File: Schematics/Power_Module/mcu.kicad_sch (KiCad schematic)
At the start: 39 parts, among them J1 USB_C_Female_USB2_Small, J4 SWD_B, J5 Stack Male Edge Connector, SW1 SW_STM_BOOT_MODE, SW3 SW_STM_RESET, U11 W25Q128JVS, U12 CP2102N-Axx-xQFN20, U13 ISO1044BDR, U9 STM32F103CBT6, Y1 X322516MMB4SI

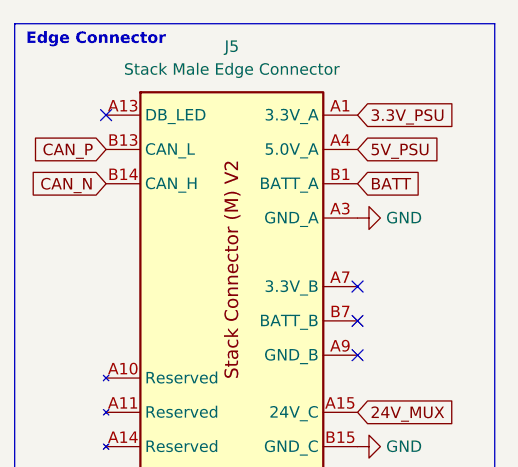
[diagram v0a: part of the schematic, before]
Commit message: adding power ORing circuit
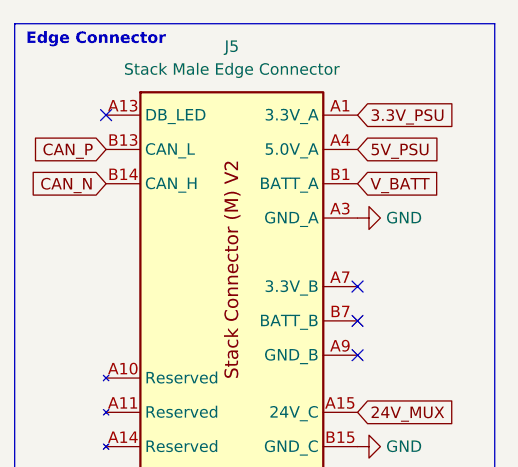
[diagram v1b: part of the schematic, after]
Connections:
- net BATT renamed V_BATT
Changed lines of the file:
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@@
 		)
 	)
-	(global_label "BATT"
+	(global_label "V_BATT"
 		(shape input)
 		(at 269.24 30.48 0)
@@
 		)
 		(property "Intersheetrefs" "${INTERSHEET_REFS}"
-			(at 276.519 30.48 0)
+			(at 278.5752 30.48 0)
 			(effects
 				(font

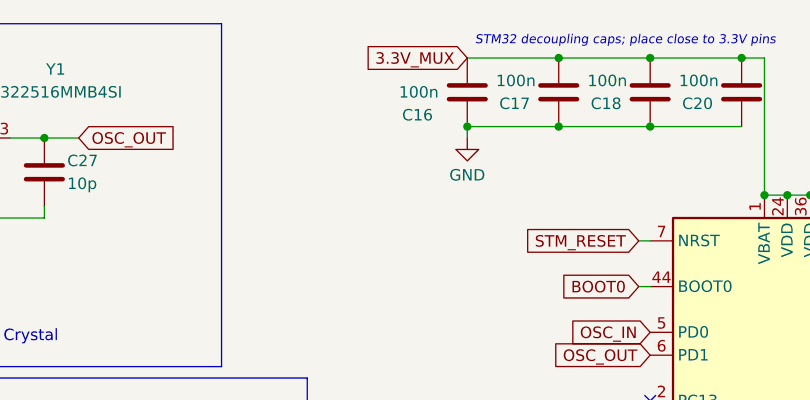
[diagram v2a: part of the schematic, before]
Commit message: Update buck designs for 500kHz, prioritize efficiency
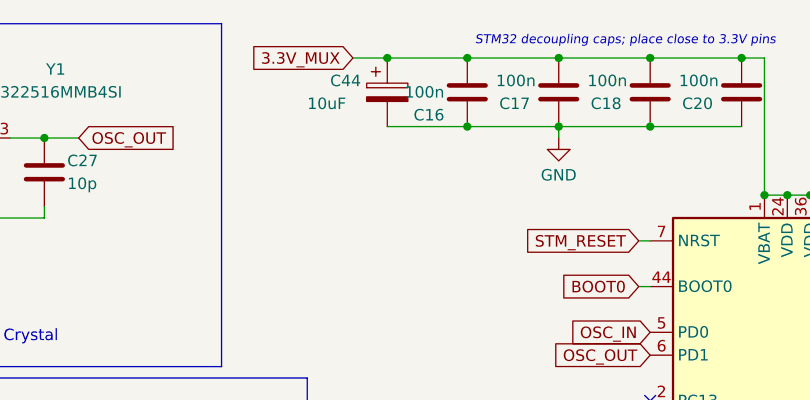
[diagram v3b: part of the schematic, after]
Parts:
- added C44: 10uF, Capacitor_SMD:CP_Elec_4x5.4, symbol Device:C_Polarized
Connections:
- net 3.3V_MUX: now also C44.1
- net GND: now also C44.2
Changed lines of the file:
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@@
 	)
 	(junction
+		(at 92.71 16.51)
+		(diameter 0)
+		(color 0 0 0 0)
+	)
+	(junction
 		(at 130.81 31.75)
 		(diameter 0)
@@
 	)
 	(junction
+		(at 83.82 16.51)
+		(diameter 0)
+		(color 0 0 0 0)
+	)
+	(junction
 		(at 113.03 24.13)
 		(diameter 0)
@@
 	(wire
 		(pts
+			(xy 83.82 16.51) (xy 92.71 16.51)
+		)
+		(stroke
+			(width 0)
+			(type default)
+		)
+	)
+	(wire
+		(pts
 			(xy 44.45 160.02) (xy 38.1 160.02)
 		)
@@
 	(wire
 		(pts
+			(xy 92.71 16.51) (xy 102.87 16.51)
+		)
+		(stroke
+			(width 0)
+			(type default)
+		)
+	)
+	(wire
+		(pts
+			(xy 83.82 24.13) (xy 92.71 24.13)
+		)
+		(stroke
+			(width 0)
+			(type default)
+		)
+	)
+	(wire
+		(pts
 			(xy 68.58 157.48) (xy 73.66 157.48)
 		)
@@
 	(wire
 		(pts
-			(xy 92.71 16.51) (xy 102.87 16.51)
+			(xy 80.01 16.51) (xy 83.82 16.51)
 		)
 		(stroke
@@
 	(wire
 		(pts
-			(xy 92.71 24.13) (xy 92.71 25.4)
+			(xy 102.87 24.13) (xy 102.87 25.4)
 		)
 		(stroke
@@
 	(global_label "3.3V_MUX"
 		(shape input)
-		(at 92.71 16.51 180)
+		(at 80.01 16.51 180)
 		(fields_autoplaced yes)
 		(effects
@@
 		)
 		(property "Intersheetrefs" "${INTERSHEET_REFS}"
-			(at 80.6534 16.51 0)
+			(at 67.9534 16.51 0)
 			(effects
 				(font
@@
 	)
 	(symbol
+		(lib_id "Device:C_Polarized")
+		(at 83.82 20.32 0)
+		(unit 1)
+		(exclude_from_sim no)
+		(in_bom yes)
+		(on_board yes)
+		(dnp no)
+		(property "Reference" "C44"
+			(at 77.47 19.05 0)
+			(effects
+				(font
+					(size 1.27 1.27)
+				)
+				(justify left)
+			)
+		)
+		(property "Value" "10uF"
+			(at 74.93 21.59 0)
+			(effects
+				(font
+					(size 1.27 1.27)
+				)
+				(justify left)
+			)
+		)
+		(property "Footprint" "Capacitor_SMD:CP_Elec_4x5.4"
+			(at 84.7852 24.13 0)
+			(effects
+				(font
+					(size 1.27 1.27)
+				)
+				(hide yes)
+			)
+		)
+		(property "Datasheet" "https://www.we-online.com/components/products/datasheet/865080340001.pdf"
+			(at 83.82 20.32 0)
+			(effects
+				(font
+					(size 1.27 1.27)
+				)
+				(hide yes)
+			)
+		)
+		(property "Description" ""
+			(at 83.82 20.32 0)
+			(effects
+				(font
+					(size 1.27 1.27)
+				)
+				(hide yes)
+			)
+		)
+		(property "Digikey" "732-8411-1-ND"
+			(at 83.82 20.32 0)
+			(effects
+				(font
+					(size 1.27 1.27)
+				)
+				(hide yes)
+			)
+		)
+		(pin "1"
+		)
+		(pin "2"
+		)
+		(instances
+			(project "Power_Module"
+				(path "/11b1f19b-ce82-4fce-baf6-0357ef2e3f24/0d4d1294-ccf0-404c-9521-5e9addbc8fbf"
+					(reference "C44")
+					(unit 1)
+				)
+			)
+		)
+	)
+	(symbol
 		(lib_id "Device:C")
 		(at 33.02 101.6 0)
@@
 		(dnp no)
 		(property "Reference" "C16"
-			(at 88.9 22.86 0)
+			(at 90.17 22.86 0)
 			(effects
 				(font
@@
 		)
 		(property "Value" "100n"
-			(at 89.535 20.32 0)
+			(at 90.17 20.32 0)
 			(effects
 				(font
@@
 	(symbol
 		(lib_id "power:GND")
-		(at 92.71 25.4 0)
+		(at 102.87 25.4 0)
 		(unit 1)
 		(exclude_from_sim no)
@@
 		(fields_autoplaced yes)
 		(property "Reference" "#PWR015"
-			(at 92.71 31.75 0)
+			(at 102.87 31.75 0)
 			(effects
 				(font
@@
 		)
 		(property "Value" "GND"
-			(at 92.71 29.5331 0)
+			(at 102.87 29.5331 0)
 			(effects
 				(font
@@
 		)
 		(property "Footprint" ""
-			(at 92.71 25.4 0)
+			(at 102.87 25.4 0)
 			(effects
 				(font
@@
 		)
 		(property "Datasheet" ""
-			(at 92.71 25.4 0)
+			(at 102.87 25.4 0)
 			(effects
 				(font
@@
 		)
 		(property "Description" ""
-			(at 92.71 25.4 0)
+			(at 102.87 25.4 0)
 			(effects
 				(font

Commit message: complete clamping and rpp for 24v gse source  - chose 24v source ORing mosfet
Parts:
- R20: JLCPCB (none) -> C31850
- R21: JLCPCB (none) -> C25819
- R22: footprint Capacitor_SMD:C_0402_1005Metric -> Resistor_SMD:R_0603_1608Metric; JLCPCB C11702 -> C21190
- U9: JLCPCB C8734 -> C8304
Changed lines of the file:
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@@
 			)
 		)
-		(property "Footprint" "Capacitor_SMD:C_0402_1005Metric"
+		(property "Footprint" "Resistor_SMD:R_0603_1608Metric"
 			(at 86.868 133.35 90)
 			(effects
@@
 			)
 		)
-		(property "JLCPCB" "C11702"
+		(property "JLCPCB" "C21190"
 			(at 85.09 133.35 0)
 			(effects
@@
 			)
 		)
-		(property "Datasheet" "http://www.winbond.com/resource-files/w25q128jv_dtr%20revc%2003272018%20plus.pdf"
+		(property "Datasheet" "${KIPRJMOD}/../../Datasheets/flashmodule_W25Q128JV-DTR_DS .pdf"
 			(at 262.89 90.17 0)
 			(effects
@@
 			)
 		)
-		(property "JLCPCB" "C8734"
+		(property "JLCPCB" "C8304"
 			(at 128.27 72.39 0)
 			(effects
@@
 			)
 		)
-		(property "JLCPCB" ""
+		(property "JLCPCB" "C31850"
 			(at 68.58 146.05 0)
 			(effects
@@
 			)
 		)
-		(property "JLCPCB" ""
+		(property "JLCPCB" "C25819 "
 			(at 68.58 153.67 0)
 			(effects

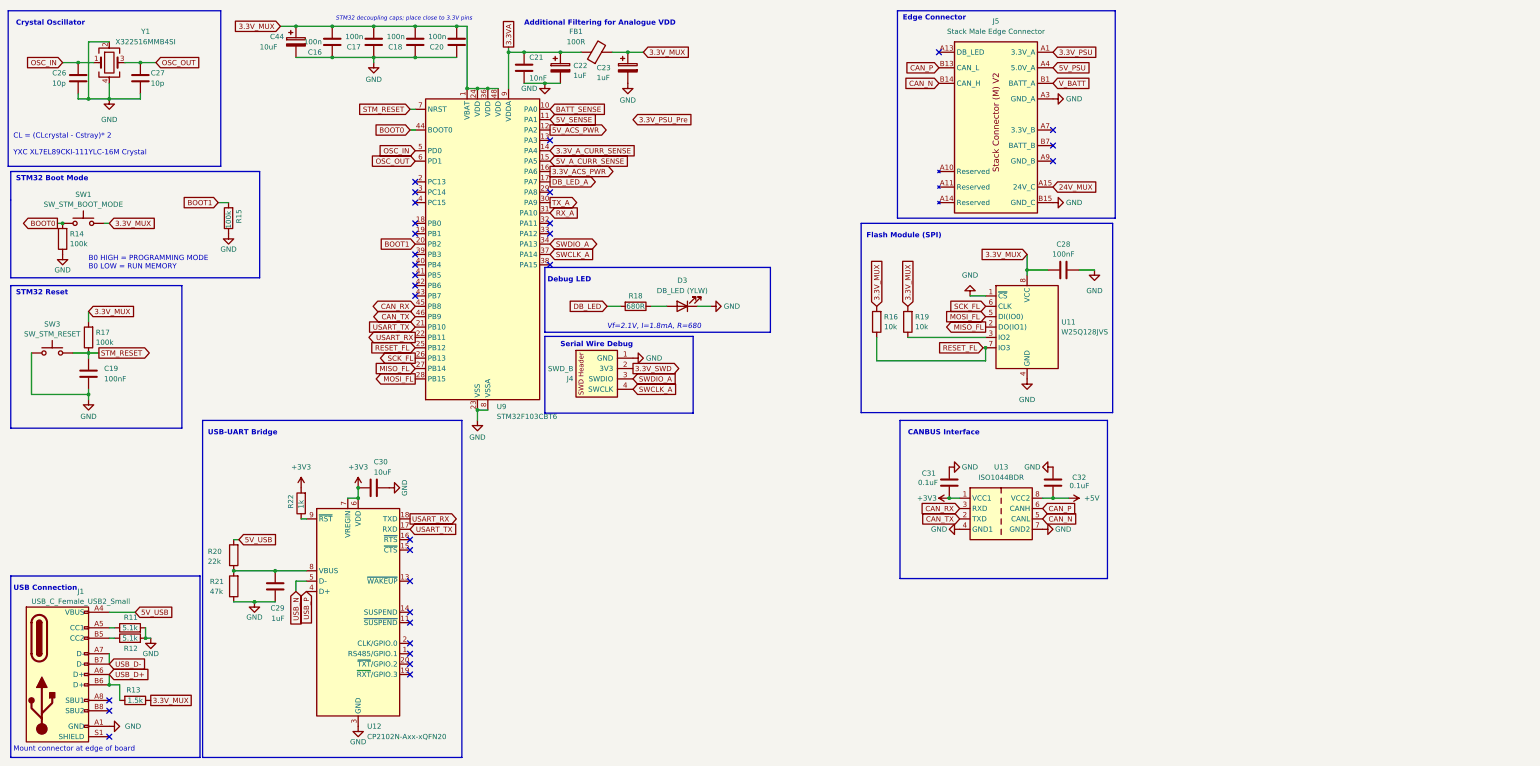
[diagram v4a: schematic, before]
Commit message: started layout design  - added shunt based 24V current sensing
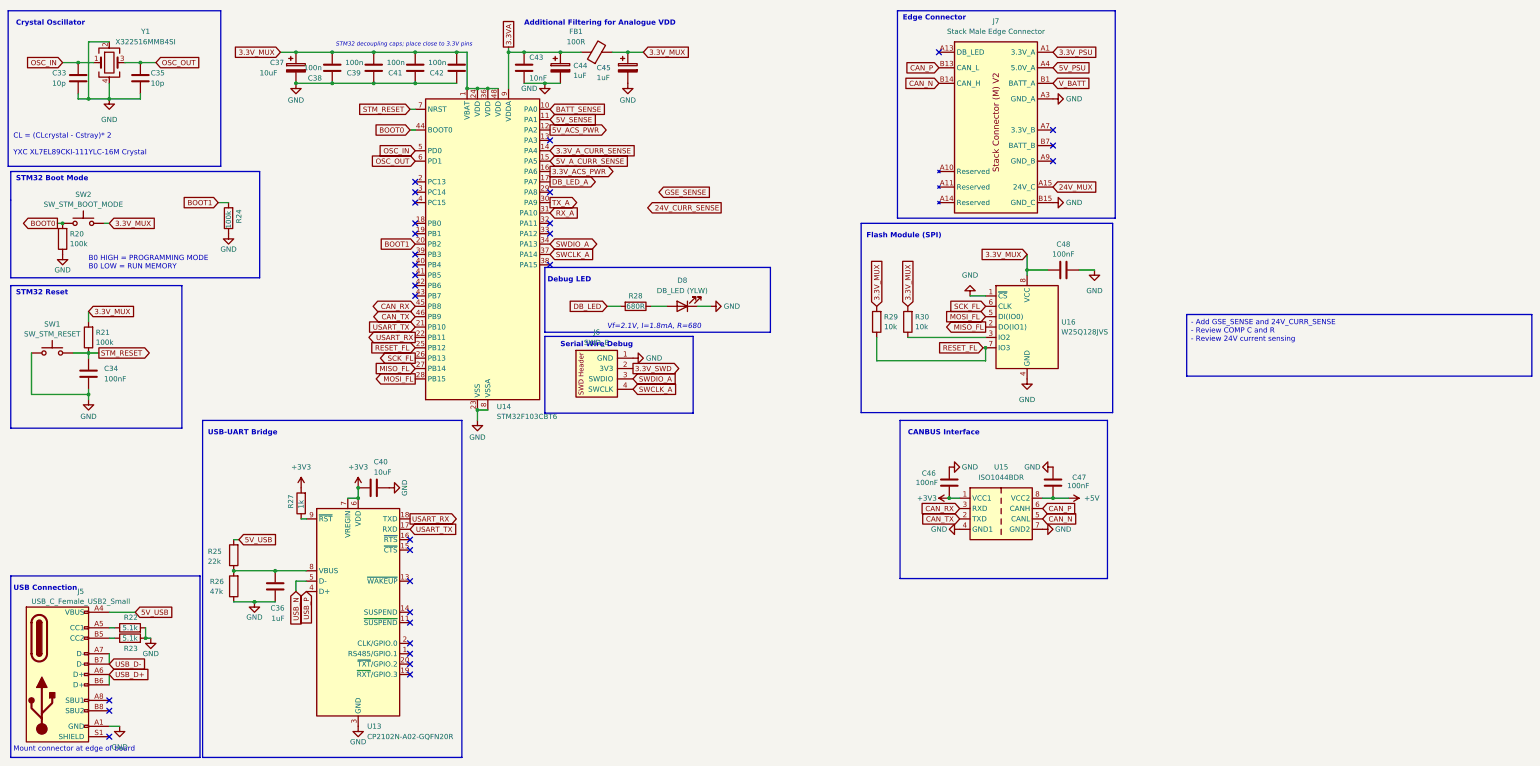
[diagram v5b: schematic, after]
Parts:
- removed R11: 5.1k, Resistor_SMD:R_0603_1608Metric, symbol Device:R
- removed R13: 1.5k, Resistor_SMD:R_0603_1608Metric, symbol Device:R
- added R22: 5.1k, Resistor_SMD:R_0603_1608Metric, symbol Device:R
- C33: renamed from C26; footprint Capacitor_SMD:C_0603_1608Metric -> Capacitor_SMD:C_0402_1005Metric; JLCPCB C1634 -> C32949
- C35: renamed from C27; footprint Capacitor_SMD:C_0603_1608Metric -> Capacitor_SMD:C_0402_1005Metric; JLCPCB C1634 -> C32949
- C46: renamed from C31; value 0.1uF -> 100nF; LCSC C14663 -> (none)
- C47: renamed from C32; value 0.1uF -> 100nF; LCSC C14663 -> (none)
- U13: renamed from U12; value CP2102N-Axx-xQFN20 -> CP2102N-A02-GQFN20R; footprint CP2102N_A02_GQFN20:QFN20_CP2102N_SIL -> digikey-footprints:QFN-20-1EP_3x3mm
- U15: renamed from U13; footprint ul_ISO1044BDR:SOIC_1044BDR_TEX -> ISO1044:SOIC_1044BDR_TEX; JLCPCB (none) -> C2878225; LCSC C2878225 -> (none)
- renumbered C19 to C34, C29 to C36, C44 to C37, C16 to C38, C17 to C39, C30 to C40, C18 to C41, C20 to C42, C21 to C43, C22 to C44, C23 to C45, C28 to C48, D3 to D8, J1 to J5, J4 to J6, J5 to J7, R14 to R20, R17 to R21, R12 to R23, R15 to R24, R20 to R25, R21 to R26, R22 to R27, R18 to R28, R16 to R29, R19 to R30, SW3 to SW1, SW1 to SW2, U9 to U14, U11 to U16
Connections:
- net GND: now also R22.2
- net at J5.A5 (CC1): now also R22.1
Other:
- moved on the sheet: C37, C38, C39, C41, C42

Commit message: current progress on power board
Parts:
- removed C37: 10uF, Capacitor_SMD:CP_Elec_4x5.4, symbol Device:C_Polarized
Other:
- note added: "moved 10uF cap next to ideal diodes"
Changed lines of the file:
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@@
 	)
 	(junction
-		(at 83.82 30.48)
-		(diameter 0)
-		(color 0 0 0 0)
-	)
-	(junction
 		(at 113.03 22.86)
 		(diameter 0)
@@
 	)
 	(junction
-		(at 83.82 22.86)
-		(diameter 0)
-		(color 0 0 0 0)
-	)
-	(junction
 		(at 113.03 30.48)
 		(diameter 0)
@@
 	(wire
 		(pts
-			(xy 83.82 30.48) (xy 92.71 30.48)
-		)
-		(stroke
-			(width 0)
-			(type default)
-		)
-	)
-	(wire
-		(pts
 			(xy 252.73 98.425) (xy 252.73 95.25)
 		)
@@
 		)
 	)
+	(wire
+		(pts
+			(xy 92.71 31.75) (xy 92.71 30.48)
+		)
+		(stroke
+			(width 0)
+			(type default)
+		)
+	)
 	(polyline
 		(pts
@@
 	(wire
 		(pts
-			(xy 83.82 22.86) (xy 92.71 22.86)
+			(xy 80.01 22.86) (xy 92.71 22.86)
 		)
 		(stroke
@@
 	(wire
 		(pts
-			(xy 80.01 22.86) (xy 83.82 22.86)
+			(xy 68.58 149.86) (xy 78.74 149.86)
 		)
 		(stroke
@@
 	(wire
 		(pts
-			(xy 68.58 149.86) (xy 78.74 149.86)
+			(xy 148.59 46.99) (xy 146.05 46.99)
 		)
 		(stroke
@@
 		)
 	)
-	(text_box " - Add GSE_SENSE and 24V_CURR_SENSE\n - Review COMP C and R\n - Review 24V current sensing"
-		(exclude_from_sim no)
-		(at 301.9806 87.0966 0)
-		(size 84.5312 15.0876)
-		(stroke
-			(width 0)
-			(type default)
-		)
-		(fill
-			(type none)
-		)
-		(effects
-			(font
-				(size 1.27 1.27)
-			)
-			(justify left top)
-		)
-	)
 	(text "STM32 Reset"
 		(exclude_from_sim no)
@@
 		)
 	)
+	(text "moved 10uF cap next \nto ideal diodes"
+		(exclude_from_sim no)
+		(at 71.12 26.67 0)
+		(effects
+			(font
+				(size 0.762 0.762)
+			)
+			(justify left)
+		)
+	)
 	(text "STM32 Boot Mode"
 		(exclude_from_sim no)
@@
 	(global_label "3.3V_A_CURR_SENSE"
 		(shape input)
-		(at 146.05 46.99 0)
+		(at 148.59 46.99 0)
 		(fields_autoplaced yes)
 		(effects
@@
 		)
 		(property "Intersheetrefs" "${INTERSHEET_REFS}"
-			(at 168.327 46.99 0)
+			(at 170.867 46.99 0)
 			(effects
 				(font
@@
 	)
 	(symbol
-		(lib_id "Device:C_Polarized")
-		(at 83.82 26.67 0)
-		(unit 1)
-		(exclude_from_sim no)
-		(in_bom yes)
-		(on_board yes)
-		(dnp no)
-		(property "Reference" "C37"
-			(at 77.47 25.4 0)
-			(effects
-				(font
-					(size 1.27 1.27)
-				)
-				(justify left)
-			)
-		)
-		(property "Value" "10uF"
-			(at 74.93 27.94 0)
-			(effects
-				(font
-					(size 1.27 1.27)
-				)
-				(justify left)
-			)
-		)
-		(property "Footprint" "Capacitor_SMD:CP_Elec_4x5.4"
-			(at 84.7852 30.48 0)
-			(effects
-				(font
-					(size 1.27 1.27)
-				)
-				(hide yes)
-			)
-		)
-		(property "Datasheet" "https://www.we-online.com/components/products/datasheet/865080340001.pdf"
-			(at 83.82 26.67 0)
-			(effects
-				(font
-					(size 1.27 1.27)
-				)
-				(hide yes)
-			)
-		)
-		(property "Description" ""
-			(at 83.82 26.67 0)
-			(effects
-				(font
-					(size 1.27 1.27)
-				)
-				(hide yes)
-			)
-		)
-		(property "Digikey" "732-8411-1-ND"
-			(at 83.82 26.67 0)
-			(effects
-				(font
-					(size 1.27 1.27)
-				)
-				(hide yes)
-			)
-		)
-		(pin "1"
-		)
-		(pin "2"
-		)
-		(instances
-			(project "Power_Module"
-				(path "/11b1f19b-ce82-4fce-baf6-0357ef2e3f24/0d4d1294-ccf0-404c-9521-5e9addbc8fbf"
-					(reference "C37")
-					(unit 1)
-				)
-			)
-		)
-	)
-	(symbol
 		(lib_id "Device:C")
 		(at 33.02 101.6 0)
@@
 	(symbol
 		(lib_id "power:GND")
-		(at 83.82 30.48 0)
+		(at 92.71 31.75 0)
 		(unit 1)
 		(exclude_from_sim no)
@@
 		(fields_autoplaced yes)
 		(property "Reference" "#PWR43"
-			(at 83.82 36.83 0)
+			(at 92.71 38.1 0)
 			(effects
 				(font
@@
 		)
 		(property "Value" "GND"
-			(at 83.82 34.6131 0)
+			(at 92.71 35.8831 0)
 			(effects
 				(font
@@
 		)
 		(property "Footprint" ""
-			(at 83.82 30.48 0)
+			(at 92.71 31.75 0)
 			(effects
 				(font
@@
 		)
 		(property "Datasheet" ""
-			(at 83.82 30.48 0)
+			(at 92.71 31.75 0)
 			(effects
 				(font
@@
 		)
 		(property "Description" ""
-			(at 83.82 30.48 0)
+			(at 92.71 31.75 0)
 			(effects
 				(font
